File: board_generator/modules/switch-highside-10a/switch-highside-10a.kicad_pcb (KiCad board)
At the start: 2 copper layers, 22.9 x 20.3 mm, 7 parts, among them J1 Screw_Terminal_01x01, Q1 NTR5103N, U1 AUIPS7111S, X1 interface, X2 interface

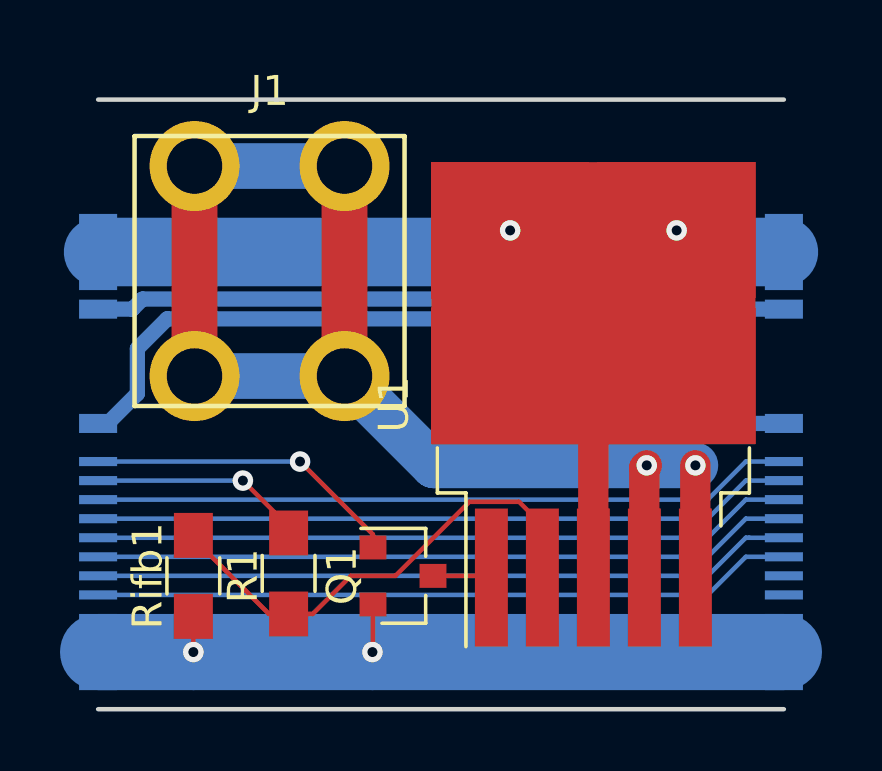
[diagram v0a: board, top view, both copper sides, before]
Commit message: Adding pull-down on switch-highside-10a to disable output by default
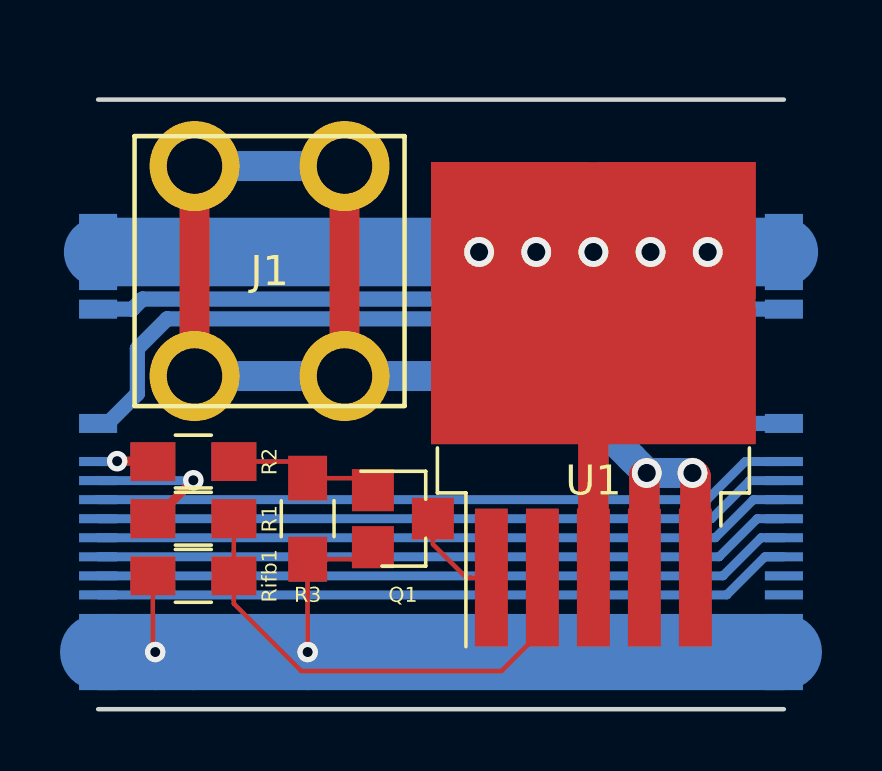
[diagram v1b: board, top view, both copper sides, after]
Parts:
- added R2: 100, Resistors_SMD:R_0805_HandSoldering, F.Cu at (134.6, 116.8)
- added R3: 10K, Resistors_SMD:R_0805_HandSoldering, F.Cu at (138.4, 118.7)
- moved R1 3.66 mm to (134.6, 118.7), turned to 180 degrees
- moved Q1 1.91 mm to (141.6, 118.7)
- turned Rifb1 to 180 degrees
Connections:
- X1 pad 5: Net-(Q1-Pad1) -> Net-(R2-Pad2)
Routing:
- net Net-(Q1-Pad1): track 10.6 -> 5.03 mm, vias 1 -> 0
- net GND: track 25.6 -> 30.9 mm
- net Net-(R1-Pad2): track 7.20 -> 5.07 mm
- net Net-(R2-Pad2): track 0.00 -> 1.84 mm, vias 0 -> 1
- net Net-(Q1-Pad3): track 1.97 -> 3.35 mm
- net +12V: vias 2 -> 5
